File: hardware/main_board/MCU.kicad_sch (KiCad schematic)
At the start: 20 parts, among them IC301 M0G3507QDGS32RQ1, J301 Conn_01x03_Pin, J302 Conn_01x06_Pin, SW301 RESET, U301 LP-MSPM0G3507

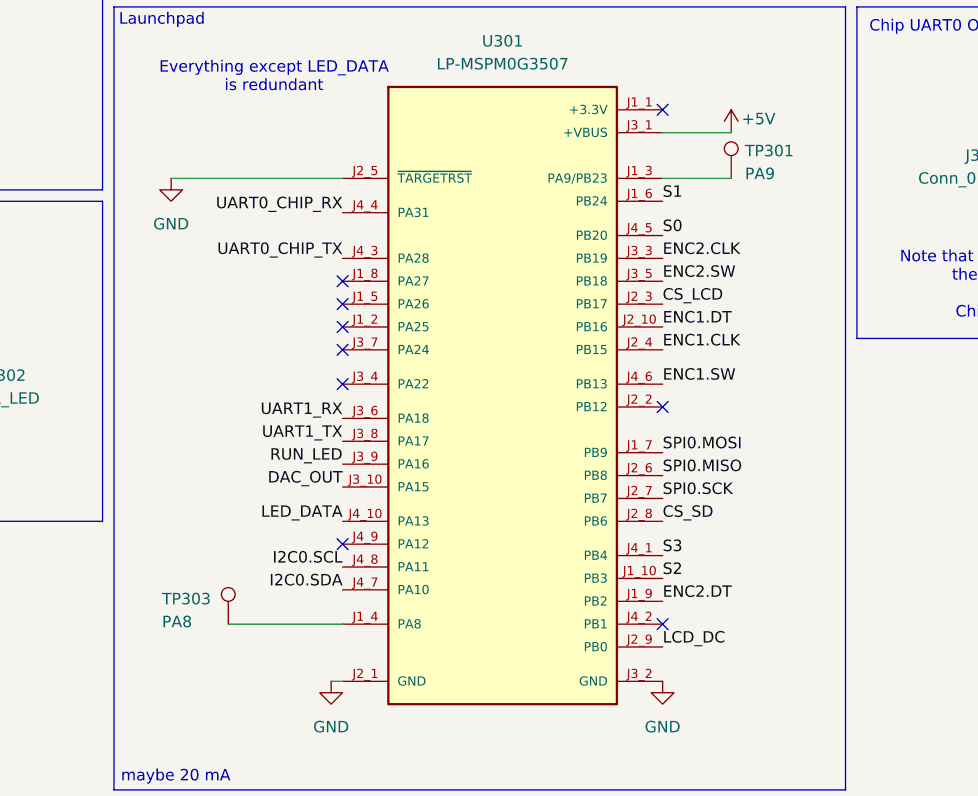
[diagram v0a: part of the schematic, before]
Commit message: changed level shifter. bunch of aesthetic changes. led resistors changed on main board. saving before nuke mouser.co.uk
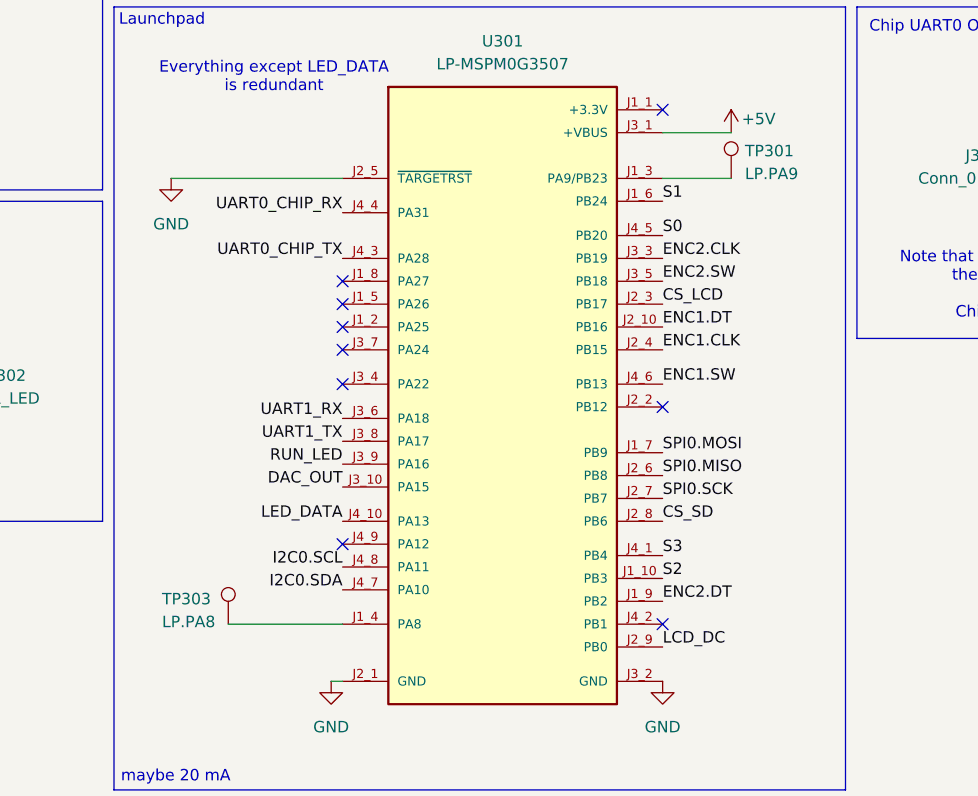
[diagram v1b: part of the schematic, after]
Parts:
- TP301: value PA9 -> LP.PA9
- TP303: value PA8 -> LP.PA8
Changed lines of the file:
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@@
 			)
 		)
-		(property "Value" "PA9"
+		(property "Value" "LP.PA9"
 			(at 129.794 106.172 0)
 			(effects
@@
 			)
 		)
-		(property "Value" "PA8"
+		(property "Value" "LP.PA8"
 			(at 65.024 155.956 0)
 			(effects

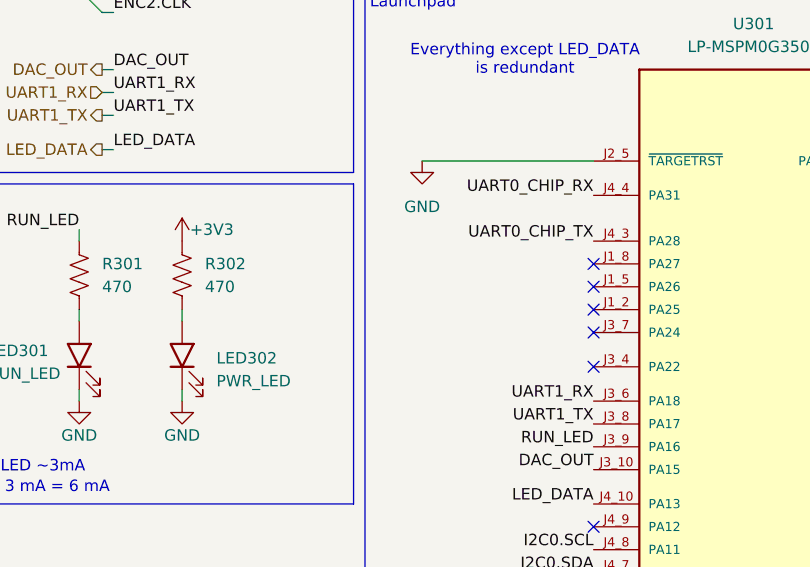
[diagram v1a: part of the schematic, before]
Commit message: finished everything except bom information. drc verification
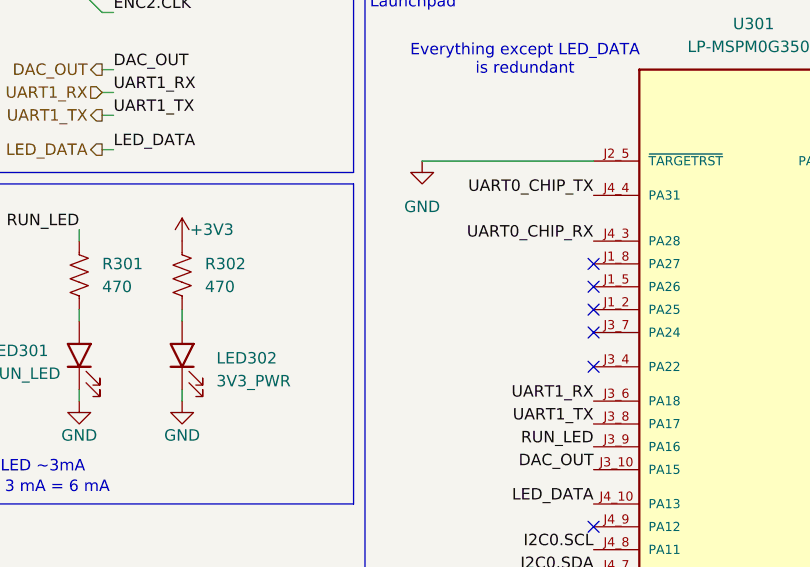
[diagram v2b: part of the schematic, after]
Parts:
- LED301: Mouser Price/Stock https://www.mouser.co.uk/ProductDetail/ams-OSRAM/LS-R976-NR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 -> https://www.mouser.com/ProductDetail/ams-OSRAM/LS-R976-NR-1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
- LED302: value PWR_LED -> 3V3_PWR; Mouser Price/Stock https://www.mouser.co.uk/ProductDetail/ams-OSRAM/LS-R976-NR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 -> https://www.mouser.com/ProductDetail/ams-OSRAM/LS-R976-NR-1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
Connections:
- net UART0_CHIP_RX: now also U301.J4_3 (PA28); no longer U301.J4_4 (PA31)
- net UART0_CHIP_TX: now also U301.J4_4 (PA31); no longer U301.J4_3 (PA28)
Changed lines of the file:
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@@
 	)
 	(label "UART0_CHIP_RX"
-		(at 85.09 110.49 180)
+		(at 85.09 115.57 180)
 		(effects
 			(font
@@
 	)
 	(label "UART0_CHIP_TX"
-		(at 85.09 115.57 180)
+		(at 85.09 110.49 180)
 		(effects
 			(font
@@
 			)
 		)
-		(property "Mouser Price/Stock" "https://www.mouser.co.uk/ProductDetail/ams-OSRAM/LS-R976-NR-1?qs=K5ta8V%252BWhtZhvCAe1sTZFg%3D%3D"
+		(property "Mouser Price/Stock" "https://www.mouser.com/ProductDetail/ams-OSRAM/LS-R976-NR-1?qs=K5ta8V%252BWhtZhvCAe1sTZFg%3D%3D"
 			(at 41.91 721.92 0)
 			(effects
@@
 			)
 		)
-		(property "Value" "PWR_LED"
+		(property "Value" "3V3_PWR"
 			(at 43.18 131.1274 0)
 			(effects
@@
 			)
 		)
-		(property "Mouser Price/Stock" "https://www.mouser.co.uk/ProductDetail/ams-OSRAM/LS-R976-NR-1?qs=K5ta8V%252BWhtZhvCAe1sTZFg%3D%3D"
+		(property "Mouser Price/Stock" "https://www.mouser.com/ProductDetail/ams-OSRAM/LS-R976-NR-1?qs=K5ta8V%252BWhtZhvCAe1sTZFg%3D%3D"
 			(at 53.34 721.92 0)
 			(effects

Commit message: led info
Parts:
- C301: Mouser Price/Stock (none) -> https://www.mouser.com/ProductDetail/KEMET/C0805C103K1RAC74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
- C302, C304, C305: Mouser Price/Stock (none) -> https://www.mouser.com/ProductDetail/Samsung-Electro-Mechan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
- C303: Mouser Price/Stock (none) -> https://www.mouser.com/ProductDetail/Walsin/MG21B104K500CT?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
- LED301: Mouser Price/Stock https://www.mouser.com/ProductDetail/ams-OSRAM/LS-R976-NR-1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 -> https://www.mouser.com/ProductDetail/LITEON/LTST-C171TBKT?q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
- LED302: Mouser Price/Stock https://www.mouser.com/ProductDetail/ams-OSRAM/LS-R976-NR-1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 -> https://www.mouser.com/ProductDetail/LITEON/LTST-C170GKT?qs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
- R301, R302: Mouser Price/Stock (none) -> https://www.mouser.com/ProductDetail/YAGEO/AF0805JR-07470RL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
- R303: Mouser Price/Stock (none) -> https://www.mouser.com/ProductDetail/YAGEO/RC0805JR-7W47KL?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
- R304, R305: Mouser Price/Stock (none) -> https://www.mouser.com/ProductDetail/YAGEO/RV0805JR-0710KL?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
- SW301, U301: now left out of the parts list
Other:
- note added: "BLU"
- note added: "GRN"
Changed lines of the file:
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@@
 		)
 	)
+	(text "GRN"
+		(exclude_from_sim no)
+		(at 46.736 133.604 0)
+		(effects
+			(font
+				(size 1.27 1.27)
+			)
+		)
+	)
 	(text "LEDs"
 		(exclude_from_sim no)
@@
 		)
 	)
+	(text "BLU"
+		(exclude_from_sim no)
+		(at 21.59 132.842 0)
+		(effects
+			(font
+				(size 1.27 1.27)
+			)
+		)
+	)
 	(text "SPI0_CS0"
 		(exclude_from_sim no)
@@
 			)
 		)
+		(property "Mouser Price/Stock" "https://www.mouser.com/ProductDetail/YAGEO/AF0805JR-07470RL?qs=tggtontpCXOaQg0VhtuXeg%3D%3D"
+			(at 39.37 119.38 0)
+			(effects
+				(font
+					(size 1.27 1.27)
+				)
+				(hide yes)
+			)
+		)
 		(pin "1"
 		)
@@
 		(unit 1)
 		(exclude_from_sim no)
-		(in_bom yes)
+		(in_bom no)
 		(on_board yes)
 		(dnp no)
@@
 			)
 		)
-		(property "Datasheet" "https://datasheet.datasheetarchive.com/originals/distributors/DKDS-18/344792.pdf"
+		(property "Datasheet" ""
 			(at 41.91 321.92 0)
 			(effects
@@
 			)
 		)
-		(property "Mouser Price/Stock" "https://www.mouser.com/ProductDetail/ams-OSRAM/LS-R976-NR-1?qs=K5ta8V%252BWhtZhvCAe1sTZFg%3D%3D"
+		(property "Mouser Price/Stock" "https://www.mouser.com/ProductDetail/LITEON/LTST-C171TBKT?qs=sGAEpiMZZMv0DJfhVcWlK%252BdbpgZMtcHOavAEZj1Si14%3D"
 			(at 41.91 721.92 0)
 			(effects
@@
 			)
 		)
+		(property "Mouser Price/Stock" "https://www.mouser.com/ProductDetail/Walsin/MG21B104K500CT?qs=sGAEpiMZZMt7gvpyg0xT8jBHDtGZvLzXjlSfFWC8Jgc2tQbZi0zprA%3D%3D"
+			(at 102.87 67.31 0)
+			(effects
+				(font
+					(size 1.27 1.27)
+				)
+				(hide yes)
+			)
+		)
 		(pin "2"
 		)
@@
 			)
 		)
+		(property "Mouser Price/Stock" "https://www.mouser.com/ProductDetail/KEMET/C0805C103K1RAC7411?qs=jbRM9o5BbzN%252BKAvowF%2FE%2Fw%3D%3D"
+			(at 81.28 67.31 0)
+			(effects
+				(font
+					(size 1.27 1.27)
+				)
+				(hide yes)
+			)
+		)
 		(pin "2"
 		)
@@
 			)
 		)
+		(property "Mouser Price/Stock" "https://www.mouser.com/ProductDetail/Samsung-Electro-Mechanics/CL10B474KO8NFNC?qs=sGAEpiMZZMt7gvpyg0xT8q%2F7CsY61%2FyFTHCmY5wjL0L9D1tlR%2FUXtQ%3D%3D"
+			(at 123.19 20.32 0)
+			(effects
+				(font
+					(size 1.27 1.27)
+				)
+				(hide yes)
+			)
+		)
 		(pin "2"
 		)
@@
 			)
 		)
+		(property "Mouser Price/Stock" "https://www.mouser.com/ProductDetail/Samsung-Electro-Mechanics/CL21A106KPFNNNE?qs=sGAEpiMZZMt7gvpyg0xT8jBAVP%252BdkPhuUJvUBe19zr8%3D"
+			(at 92.71 67.31 0)
+			(effects
+				(font
+					(size 1.27 1.27)
+				)
+				(hide yes)
+			)
+		)
 		(pin "2"
 		)
@@
 			)
 		)
-		(property "Datasheet" "https://datasheet.datasheetarchive.com/originals/distributors/DKDS-18/344792.pdf"
+		(property "Datasheet" ""
 			(at 53.34 321.92 0)
 			(effects
@@
 			)
 		)
-		(property "Mouser Price/Stock" "https://www.mouser.com/ProductDetail/ams-OSRAM/LS-R976-NR-1?qs=K5ta8V%252BWhtZhvCAe1sTZFg%3D%3D"
+		(property "Mouser Price/Stock" "https://www.mouser.com/ProductDetail/LITEON/LTST-C170GKT?qs=sGAEpiMZZMv0DJfhVcWlK%252BdbpgZMtcHOLj2jKamJQec%3D"
 			(at 53.34 721.92 0)
 			(effects
@@
 			)
 		)
+		(property "Mouser Price/Stock" "https://www.mouser.com/ProductDetail/YAGEO/RC0805JR-7W47KL?qs=tggtontpCXNoMeTIW8%252BKHA%3D%3D"
+			(at 81.28 48.26 0)
+			(effects
+				(font
+					(size 1.27 1.27)
+				)
+				(hide yes)
+			)
+		)
 		(pin "1"
 		)
@@
 			)
 		)
+		(property "Mouser Price/Stock" "https://www.mouser.com/ProductDetail/Samsung-Electro-Mechanics/CL21B105KPFNNNE?qs=349EhDEZ59rb3V94UrmRdQ%3D%3D"
+			(at 213.36 48.26 0)
+			(effects
+				(font
+					(size 1.27 1.27)
+				)
+				(hide yes)
+			)
+		)
 		(pin "2"
 		)
@@
 			)
 		)
+		(property "Mouser Price/Stock" "https://www.mouser.com/ProductDetail/YAGEO/RV0805JR-0710KL?qs=qpJ%252B%252B%252Bdg6p3bGiIDT3p%252B0w%3D%3D"
+			(at 109.22 35.56 0)
+			(effects
+				(font
+					(size 1.27 1.27)
+				)
+				(hide yes)
+			)
+		)
 		(pin "1"
 		)
@@
 			)
 		)
+		(property "Mouser Price/Stock" "https://www.mouser.com/ProductDetail/YAGEO/RV0805JR-0710KL?qs=qpJ%252B%252B%252Bdg6p3bGiIDT3p%252B0w%3D%3D"
+			(at 119.38 35.56 0)
+			(effects
+				(font
+					(size 1.27 1.27)
+				)
+				(hide yes)
+			)
+		)
 		(pin "1"
 		)
@@
 		(unit 1)
 		(exclude_from_sim no)
-		(in_bom yes)
+		(in_bom no)
 		(on_board yes)
 		(dnp no)
@@
 			(at 27.94 119.38 0)
 			(effects
+				(font
+					(size 1.27 1.27)
+				)
+				(hide yes)
+			)
+		)
+		(property "Mouser Price/Stock" "https://www.mouser.com/ProductDetail/YAGEO/AF0805JR-07470RL?qs=tggtontpCXOaQg0VhtuXeg%3D%3D"
+			(at 27.94 119.38 0)
+			(effects

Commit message: kys harddare
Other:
- note added: "MISO"
- note added: "MOSI"
- note added: "Note that if you need an external UART0 connection to the LPAD, you need to flip the connection Chip RX -> LPAD TX Chip TX -> LPAD RX"
- note added: "SCK"
- note removed: "Note that if you need an external UART0 connection to the LPAD, you need to flip the connection Chip UART0 is interfaced to LPAD UART0"
- moved on the sheet: J301
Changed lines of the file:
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@@
 		)
 	)
+	(text "MOSI"
+		(exclude_from_sim no)
+		(at 134.874 139.192 0)
+		(effects
+			(font
+				(size 1.27 1.27)
+			)
+		)
+	)
 	(text "LEDs"
 		(exclude_from_sim no)
@@
 		)
 	)
-	(text "Note that if you need an external UART0 connection to\nthe LPAD, you need to flip the connection\n\nChip UART0 is interfaced to LPAD UART0"
+	(text "Note that if you need an external UART0 connection to\nthe LPAD, you need to flip the connection\n\nChip RX -> LPAD TX\nChip TX -> LPAD RX"
 		(exclude_from_sim no)
-		(at 170.942 118.618 0)
+		(at 170.942 117.348 0)
 		(effects
 			(font
@@
 		)
 	)
+	(text "MISO"
+		(exclude_from_sim no)
+		(at 134.874 141.478 0)
+		(effects
+			(font
+				(size 1.27 1.27)
+			)
+		)
+	)
 	(text "Hierarchical Labels"
 		(exclude_from_sim no)
@@
 		)
 	)
+	(text "SCK"
+		(exclude_from_sim no)
+		(at 134.874 136.652 0)
+		(effects
+			(font
+				(size 1.27 1.27)
+			)
+		)
+	)
 	(text_box "PA0/PA1 are open drain, 5V tolerant."
 		(exclude_from_sim no)
@@
 	(wire
 		(pts
-			(xy 171.45 106.68) (xy 170.18 106.68)
+			(xy 171.45 101.6) (xy 170.18 101.6)
 		)
 		(stroke
@@
 	)
 	(label "UART0_CHIP_TX"
-		(at 170.18 104.14 0)
+		(at 170.18 99.06 0)
 		(effects
 			(font
@@
 	)
 	(label "UART0_CHIP_RX"
-		(at 170.18 101.6 0)
+		(at 170.18 96.52 0)
 		(effects
 			(font
@@
 	(symbol
 		(lib_id "Connector:Conn_01x03_Pin")
-		(at 165.1 104.14 0)
+		(at 165.1 99.06 0)
 		(unit 1)
 		(exclude_from_sim no)
@@
 		(dnp no)
 		(property "Reference" "J301"
-			(at 156.21 104.14 0)
+			(at 156.21 99.06 0)
 			(effects
 				(font
@@
 		)
 		(property "Value" "Conn_01x03_Pin"
-			(at 156.21 106.68 0)
+			(at 156.21 101.6 0)
 			(effects
 				(font
@@
 		)
 		(property "Footprint" "Connector_PinHeader_2.54mm:PinHeader_1x03_P2.54mm_Vertical"
-			(at 165.1 104.14 0)
+			(at 165.1 99.06 0)
 			(effects
 				(font
@@
 		)
 		(property "Datasheet" "~"
-			(at 165.1 104.14 0)
+			(at 165.1 99.06 0)
 			(effects
 				(font
@@
 		)
 		(property "Description" "Generic connector, single row, 01x03, script generated"
-			(at 165.1 104.14 0)
+			(at 165.1 99.06 0)
 			(effects
 				(font
@@
 	(symbol
 		(lib_id "power:GND")
-		(at 171.45 106.68 0)
+		(at 171.45 101.6 0)
 		(unit 1)
 		(exclude_from_sim no)
@@
 		(fields_autoplaced yes)
 		(property "Reference" "#PWR0314"
-			(at 171.45 113.03 0)
+			(at 171.45 107.95 0)
 			(effects
 				(font
@@
 		)
 		(property "Value" "GND"
-			(at 171.45 111.76 0)
+			(at 171.45 106.68 0)
 			(effects
 				(font
@@
 		)
 		(property "Footprint" ""
-			(at 171.45 106.68 0)
+			(at 171.45 101.6 0)
 			(effects
 				(font
@@
 		)
 		(property "Datasheet" ""
-			(at 171.45 106.68 0)
+			(at 171.45 101.6 0)
 			(effects
 				(font
@@
 		)
 		(property "Description" "Power symbol creates a global label with name \"GND\" , ground"
-			(at 171.45 106.68 0)
+			(at 171.45 101.6 0)
 			(effects
 				(font

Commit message: spi. butchered main
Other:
- note added: "SPI1.MISO"
- note added: "SPI1.MOSI"
- note added: "SPI1.SCK"
- note removed: "MISO"
- note removed: "MOSI"
- note removed: "SCK"
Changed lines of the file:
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@@
 		)
 	)
-	(text "MOSI"
+	(text "SPI1.MOSI"
 		(exclude_from_sim no)
-		(at 134.874 139.192 0)
+		(at 135.636 138.938 0)
 		(effects
 			(font
@@
 		)
 	)
-	(text "MISO"
+	(text "SPI1.MISO"
 		(exclude_from_sim no)
-		(at 134.874 141.478 0)
+		(at 135.636 141.224 0)
 		(effects
 			(font
@@
 		)
 	)
-	(text "SCK"
+	(text "SPI1.SCK"
 		(exclude_from_sim no)
-		(at 134.874 136.652 0)
+		(at 135.636 136.398 0)
 		(effects
 			(font
